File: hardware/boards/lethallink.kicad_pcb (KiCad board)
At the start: 6 copper layers, 86 x 111.1 mm, 105 parts, among them J1 PCIe-x4, J2 USB3_Micro_B_Amphenol, Q1 Q_NMOS_GSD, Q2 Q_NMOS_GSD, Q3 Q_NMOS_GSD, Q4 Q_NMOS_GSD, Q5 SI7232DN-T1-GE3, SW1 SW_DIP_x03, U1 ECP5UM5G-381caBGA, U2 ADP5050ACPZ-R7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

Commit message: Playing around with some of the PCIe power input stuff, not happy with it, I'll rip it up and try again some other time
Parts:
- added FB4: 100 @ 100MHz, Resistor_SMD:R_0603_1608Metric, F.Cu at (67.2, 115.8)
- added FB5: 100 @ 100MHz, Resistor_SMD:R_0603_1608Metric, F.Cu at (65.3, 115.8)
- added FB6: 100 @ 100MHz, Resistor_SMD:R_0603_1608Metric, F.Cu at (63.4, 115.8)
- added FB7: 100 @ 100MHz, Resistor_SMD:R_0603_1608Metric, B.Cu at (64.4, 115.8)
- added FB8: 220 @ 100Mhz, Resistor_SMD:R_0603_1608Metric, B.Cu at (70.5, 115.8)
- added FB9: 220 @ 100Mhz, Resistor_SMD:R_0603_1608Metric, B.Cu at (72.2, 115.8)
- FB1: moved to B.Cu
- moved R3 82.0 mm to (64.2, 110.5), turned to 0 degrees
- moved D3 78.8 mm to (67.0, 109.8), turned to 270 degrees
- moved R2 69.6 mm to (72.8, 110.5)
- moved D2 69.1 mm to (70.2, 109.7), turned to 270 degrees
- moved R1 67.1 mm to (74.7, 116.5), turned to 0 degrees
- moved D1 67.1 mm to (75.4, 114.0), turned to 270 degrees
- moved FB2 30.8 mm to (70.0, 115.8), turned to 270 degrees
- moved FB3 27.9 mm to (72.0, 115.8), turned to 270 degrees
- moved FB1 27.5 mm to (66.2, 115.8), turned to 90 degrees
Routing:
- net +3V3: track 0.00 -> 3.48 mm, vias 0 -> 4
- net +12V: track 2.96 -> 6.03 mm, vias 9 -> 14
- net Net-(D3-Pad2): track 0.00 -> 2.08 mm
- net Net-(D2-Pad2): track 0.00 -> 1.71 mm
- net Net-(D1-Pad2): track 0.00 -> 1.67 mm
- net +3.3VA: track 0.00 -> 1.29 mm, vias 0 -> 2
- added copper zone on B.Cu, net +12V
- added copper zone on F.Cu, net +3.3VA
- added copper zone on B.Cu, net +3V3
- added copper zone on F.Cu, net +3V3
- added copper zone on B.Cu, net Net-(FB1-Pad1)
- added copper zone on F.Cu, net Net-(FB1-Pad1)
- added copper zone on B.Cu, net Net-(FB2-Pad2)
- added copper zone on F.Cu, net Net-(FB2-Pad2)
- added copper zone on F.Cu, net Net-(FB3-Pad2)
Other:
- board text added: "12V0"
- board text added: "1V2"
- board text added: "1V5"
- board text added: "1V8"
- board text added: "2V5"
- board text added: "3V3"
- board text added: "3V3 Aux"

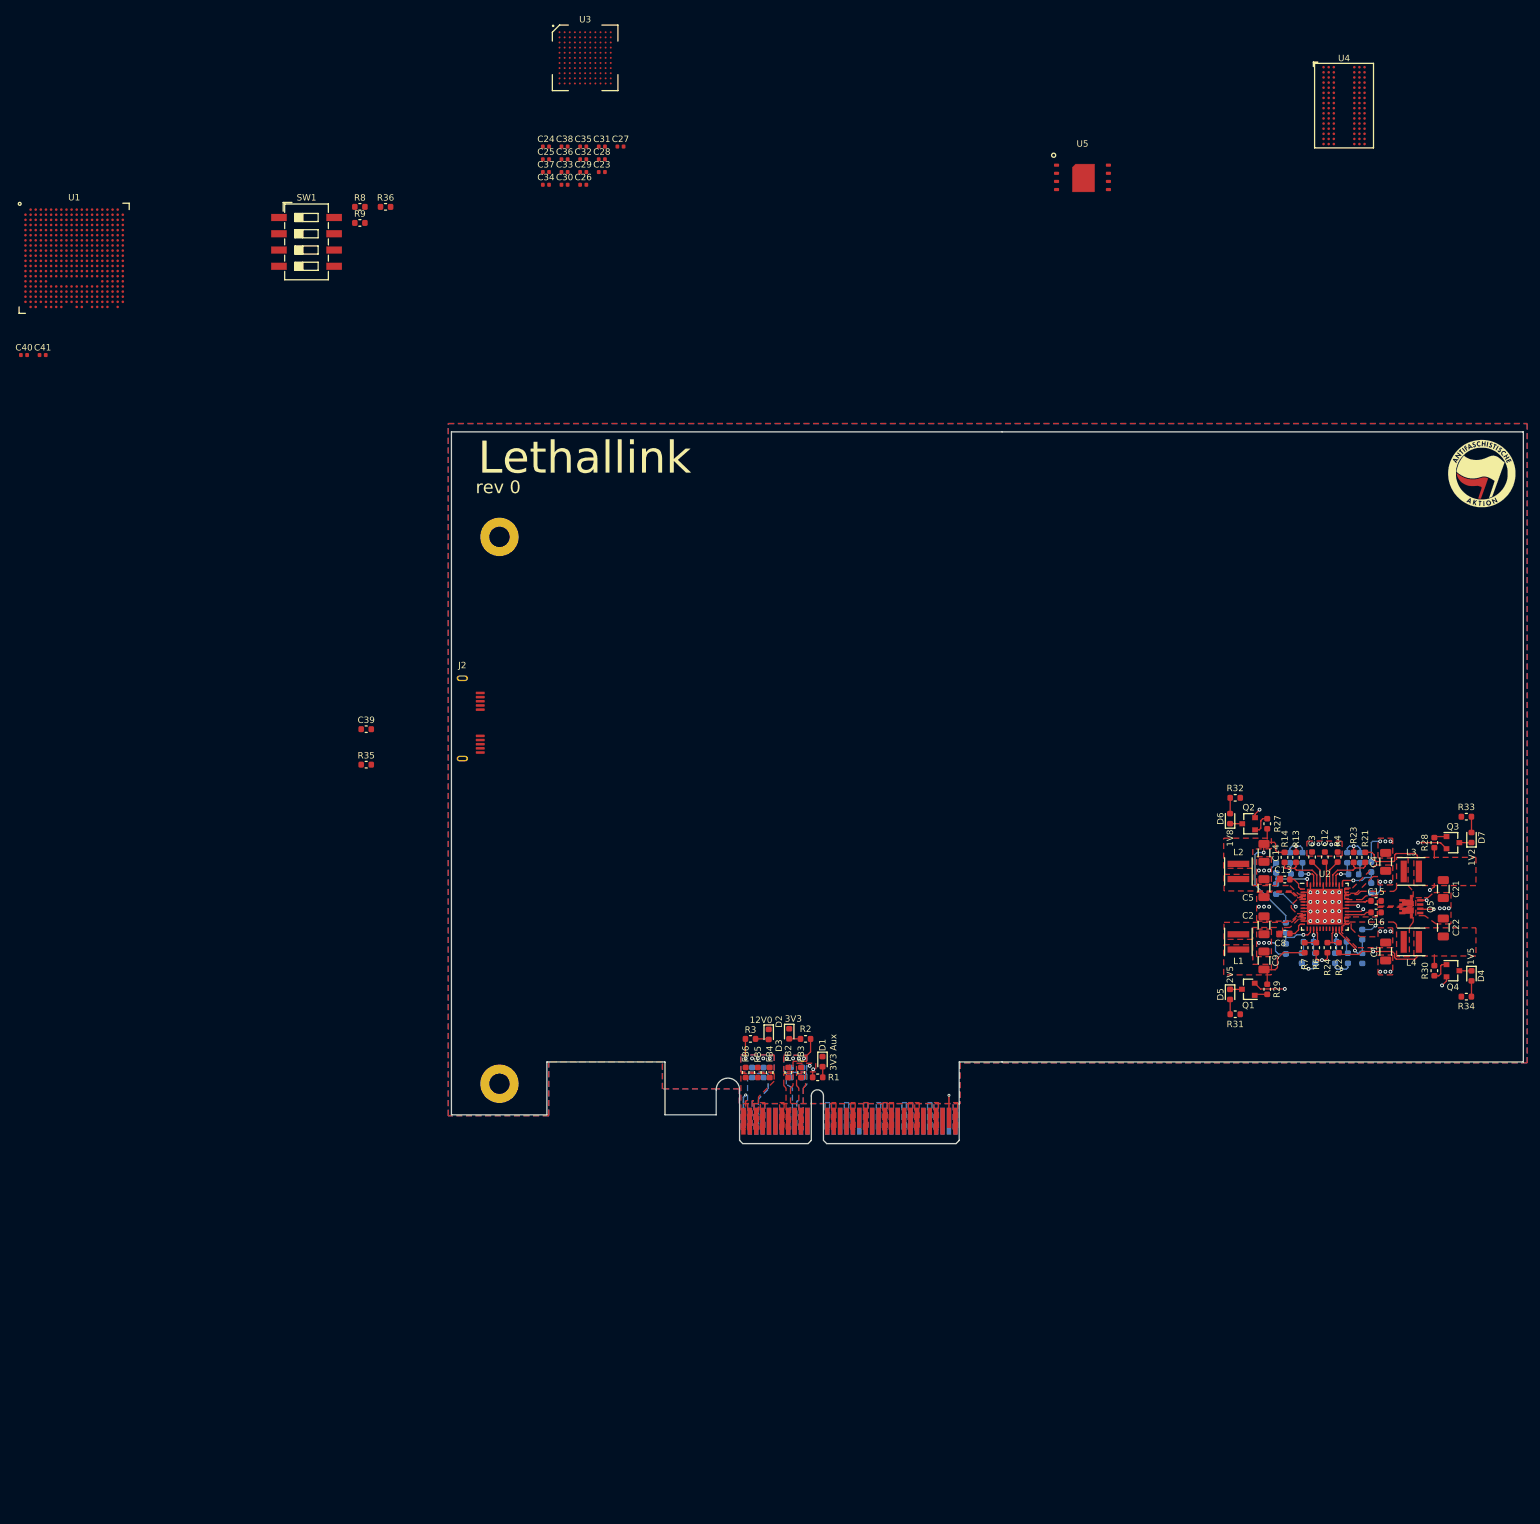
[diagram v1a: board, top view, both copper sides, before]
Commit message: Moving some things around trying to figure out where they should roughly go, Also added some isolated earth pours for the USB sheild
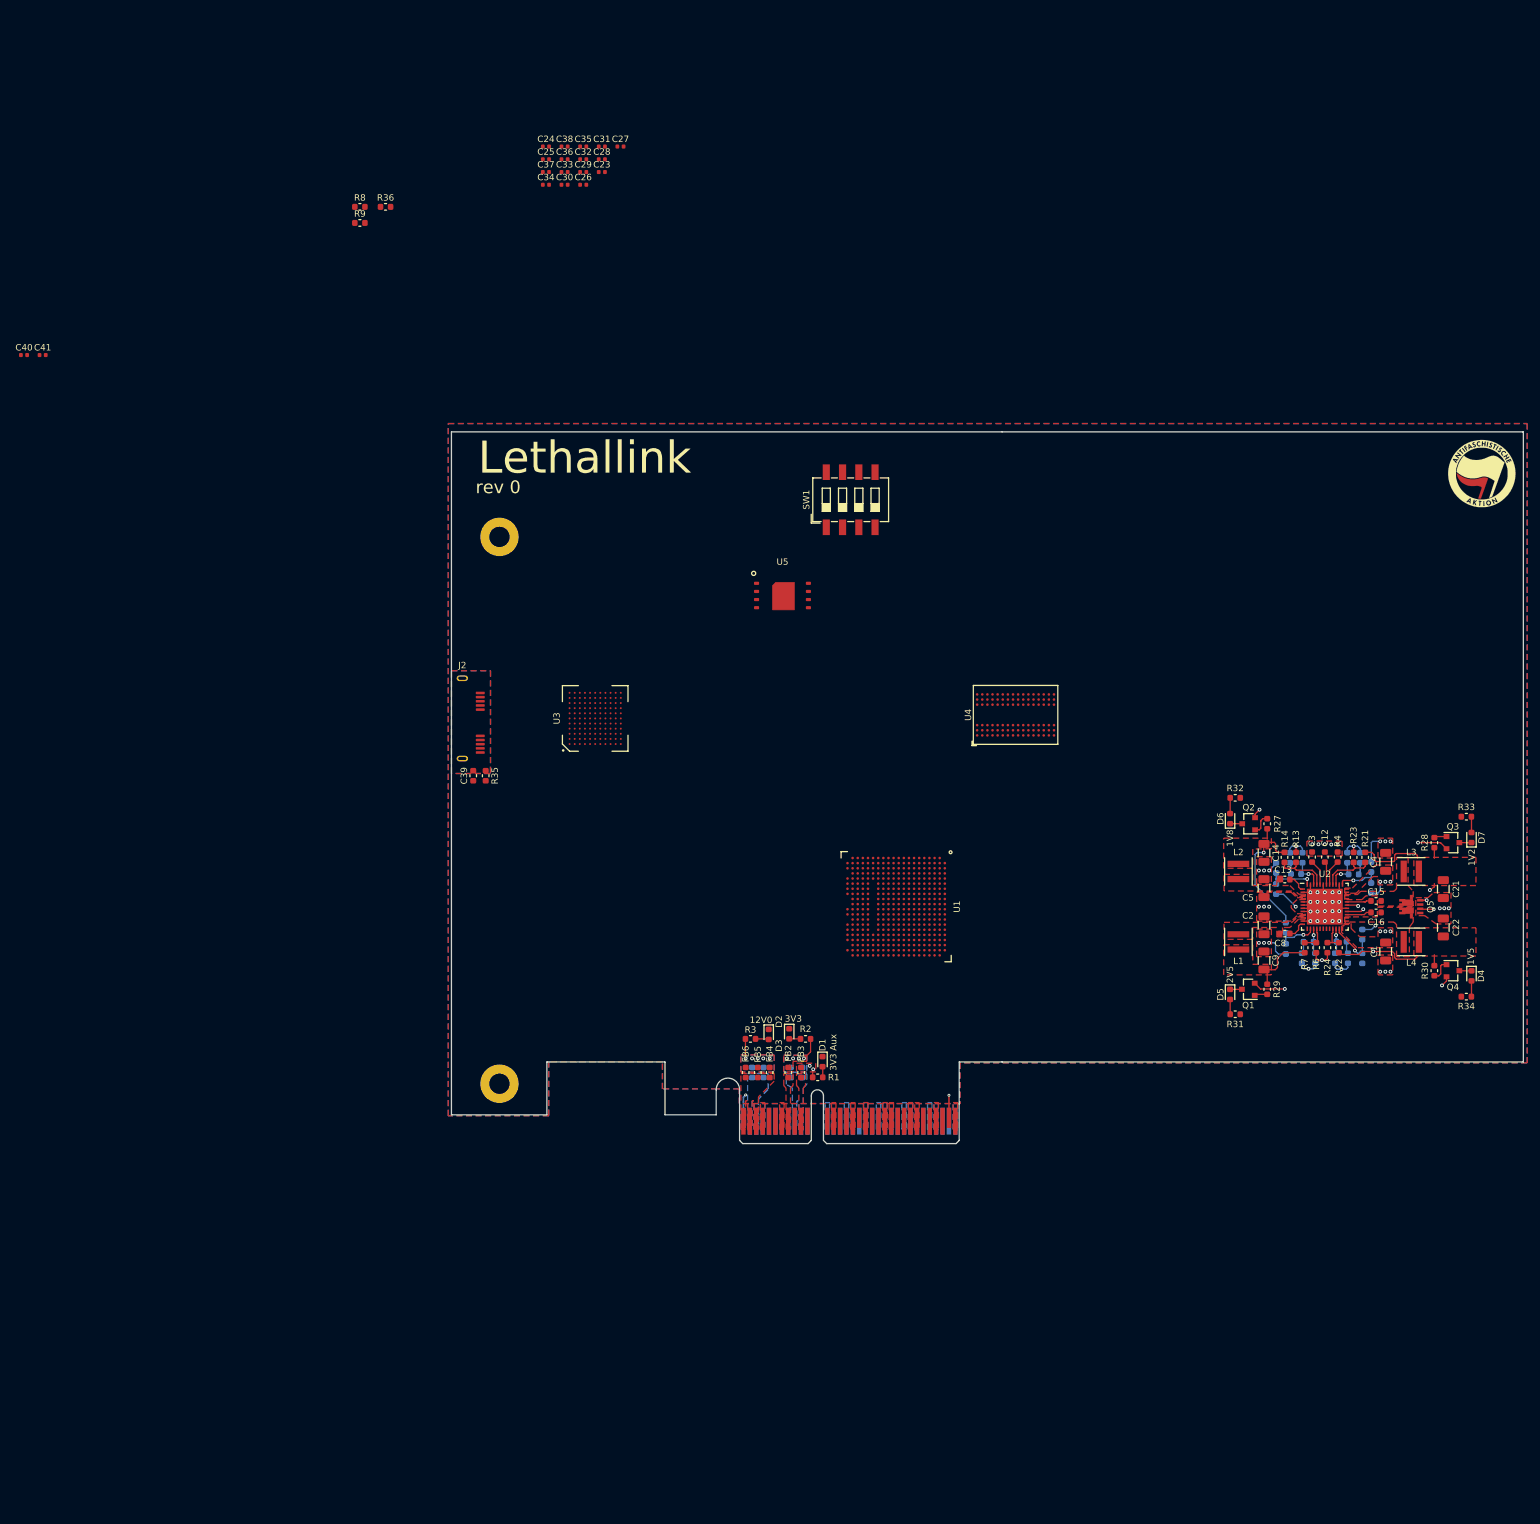
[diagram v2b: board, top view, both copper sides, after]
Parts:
- moved U1 163.5 mm to (86.9, 89.8), turned to 270 degrees
- moved U4 108.1 mm to (105.5, 59.9), turned to 90 degrees
- moved U3 103.2 mm to (39.9, 60.5), turned to 90 degrees
- moved SW1 94.0 mm to (79.8, 26.3), turned to 90 degrees
- moved U5 80.4 mm to (69.2, 41.3)
- moved R35 18.7 mm to (22.8, 69.4), turned to 270 degrees
- moved C39 18.2 mm to (20.9, 69.4), turned to 90 degrees
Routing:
- added copper zone on In4.Cu, net /PCIe Interface/TX0_P
- added copper zone on B.Cu, net Net-(C39-Pad2)
- added copper zone on F.Cu, net Net-(C39-Pad2)
- added copper zone on In1.Cu, net Net-(C39-Pad2)
- added copper zone on In2.Cu, net Net-(C39-Pad2)
- added copper zone on In3.Cu, net Net-(C39-Pad2)
